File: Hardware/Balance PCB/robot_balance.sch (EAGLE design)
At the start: 54 parts, among them P1 10118194-0001LF, Q1 16Mhz

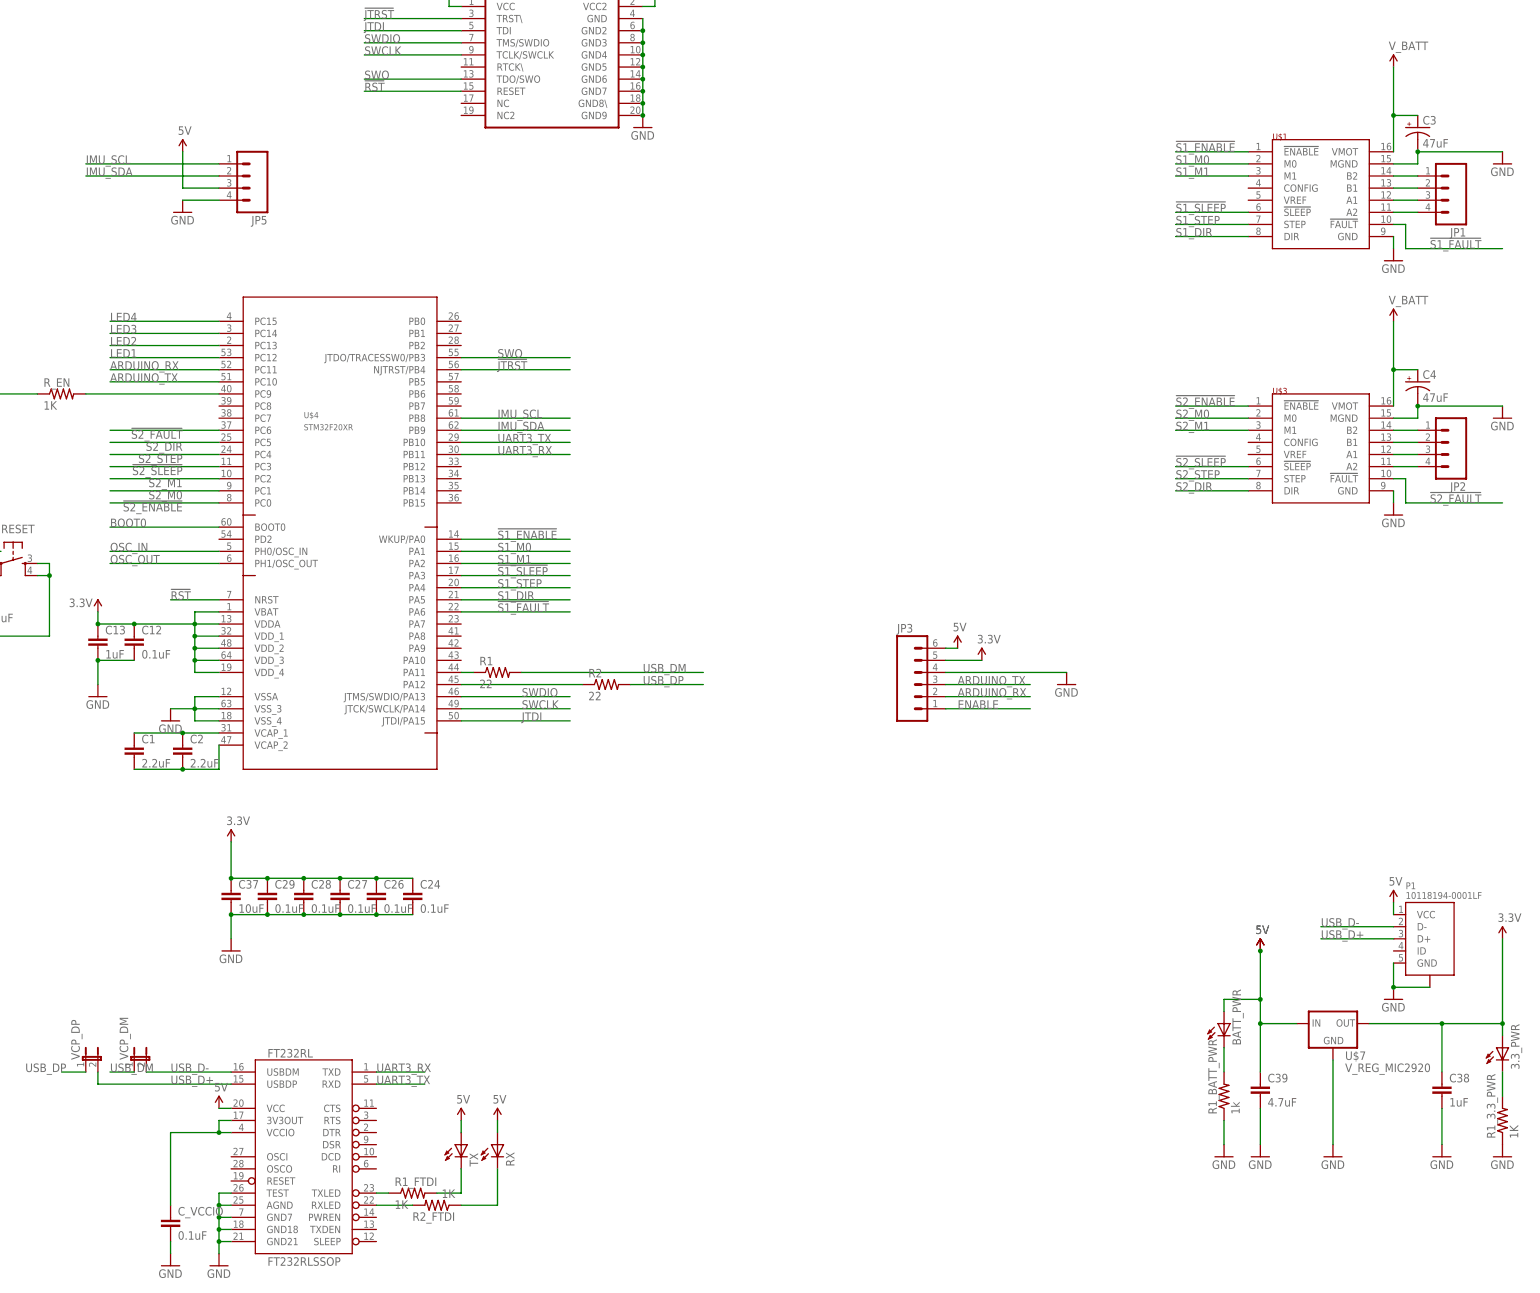
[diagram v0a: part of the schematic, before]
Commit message: Moved MPU to middle of board
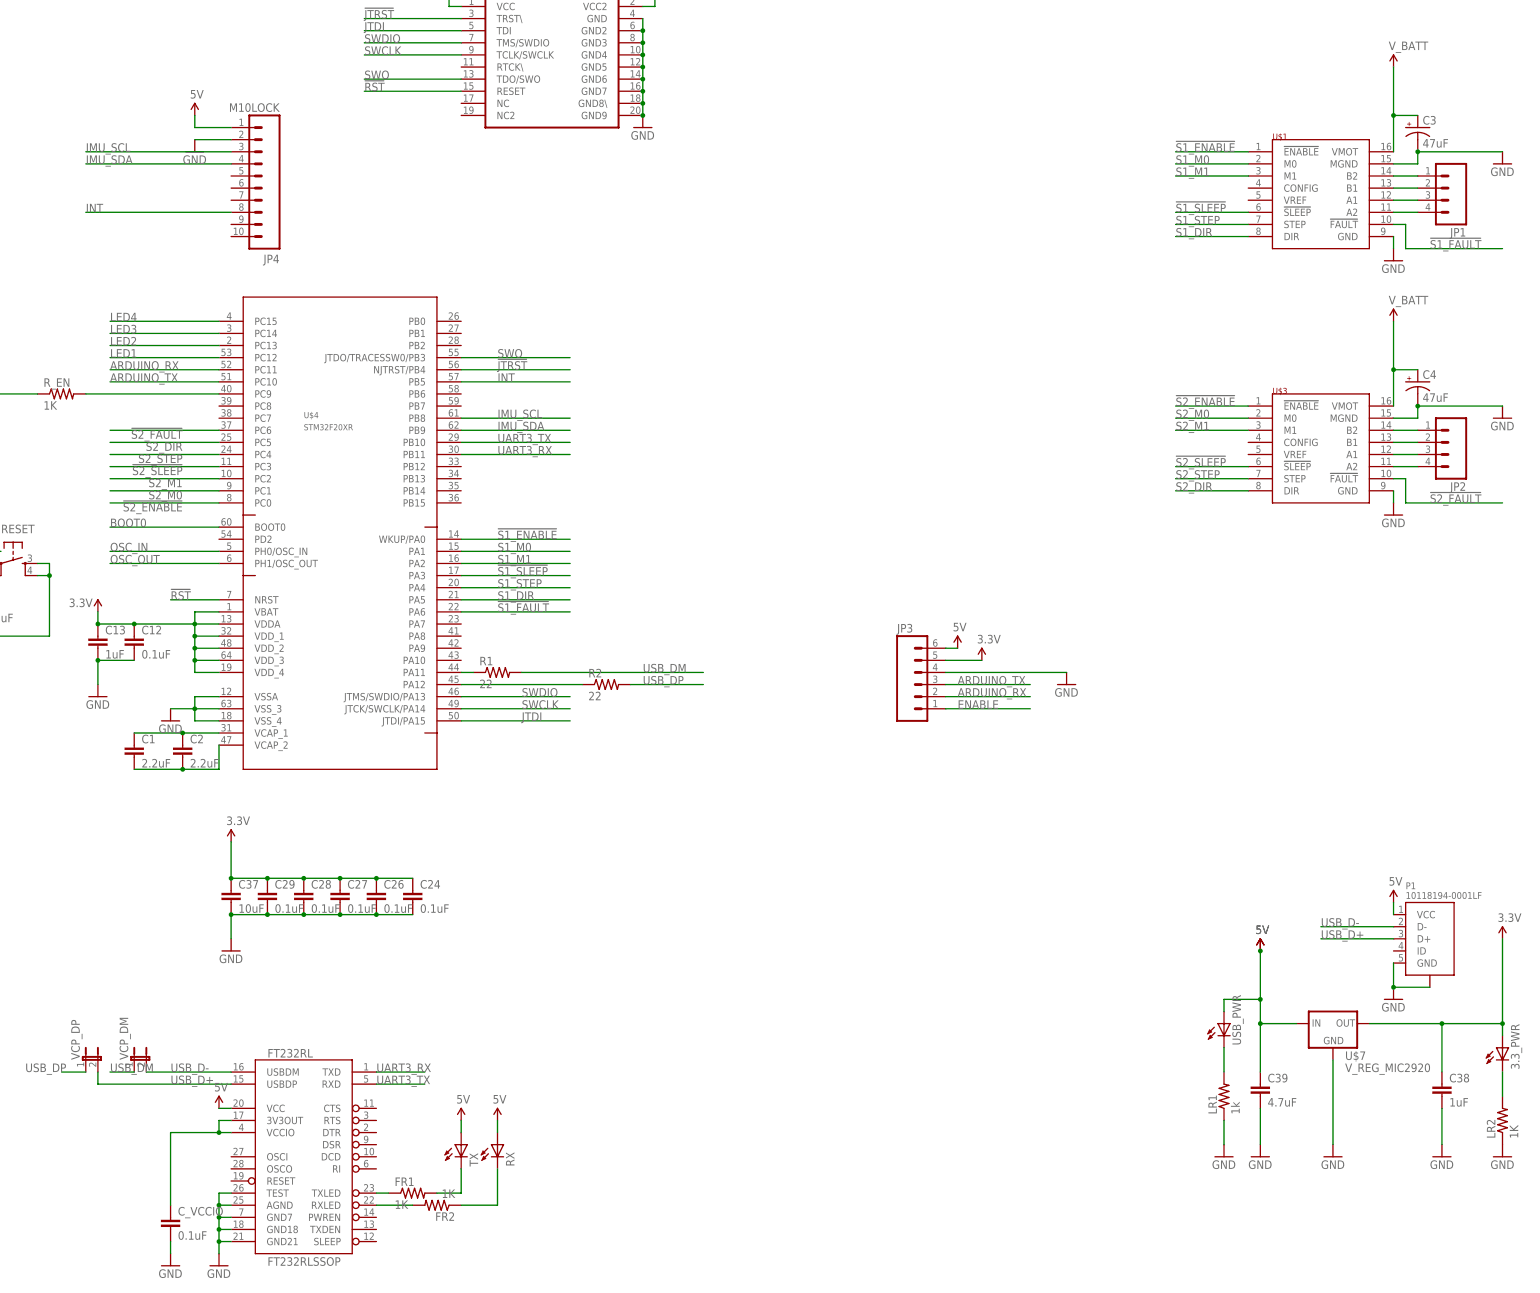
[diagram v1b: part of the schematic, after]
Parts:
- removed BATT_PWR: (no value), LilyPad-Wearables:LED1206
- removed JP5: (no value), SparkFun-Connectors:M04POLAR_LOCK
- added JP4: M10LOCK, SparkFun-Connectors:M10LOCK
- added USB_PWR: (no value), adafruit:LEDCHIP-LED0805
- renumbered R1_3.3_PWR to LR2, R1_BATT_PWR to LR1, R1_FTDI to FR1, R2_FTDI to FR2
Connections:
- new net INT: JP4.8, U$4.PB5
- net 5V: now also JP4.1, USB_PWR.A; no longer BATT_PWR.A, JP5.3
- net GND: now also JP4.2; no longer JP5.4
- net IMU_SCL: now also JP4.3; no longer JP5.1
- net IMU_SDA: now also JP4.4; no longer JP5.2
- net N$19: now also USB_PWR.C; no longer BATT_PWR.C
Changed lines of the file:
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@@
 <part name="GND20" library="SparkFun-Aesthetics" deviceset="GND" device=""/>
 <part name="SUPPLY18" library="SparkFun-Aesthetics" deviceset="3.3V" device=""/>
-<part name="BATT_PWR" library="LilyPad-Wearables" deviceset="LED" device="1206"/>
+<part name="USB_PWR" library="adafruit" deviceset="LED" device="CHIP-LED0805"/>
 <part name="3.3_PWR" library="LilyPad-Wearables" deviceset="LED" device="1206"/>
 <part name="GND22" library="SparkFun-Aesthetics" deviceset="GND" device=""/>
 <part name="GND23" library="SparkFun-Aesthetics" deviceset="GND" device=""/>
-<part name="R1_3.3_PWR" library="SparkFun-Resistors" deviceset="RESISTOR" device="0805-RES" value="1K"/>
-<part name="R1_BATT_PWR" library="SparkFun-Resistors" deviceset="RESISTOR" device="0805-RES" value="1k"/>
+<part name="LR2" library="SparkFun-Resistors" deviceset="RESISTOR" device="0805-RES" value="1K"/>
+<part name="LR1" library="SparkFun-Resistors" deviceset="RESISTOR" device="0805-RES" value="1k"/>
 <part name="U$7" library="SparkFun-PowerIC" deviceset="V_REG_MIC2920" device=""/>
 <part name="C39" library="SparkFun-Capacitors" deviceset="22UF-6.3V-20%(0805)" device="" value="4.7uF"/>
@@
 <part name="GND6" library="SparkFun-Aesthetics" deviceset="GND" device=""/>
 <part name="GND7" library="SparkFun-Aesthetics" deviceset="GND" device=""/>
-<part name="JP5" library="SparkFun-Connectors" deviceset="M04" device="POLAR_LOCK"/>
 <part name="GND9" library="SparkFun-Aesthetics" deviceset="GND" device=""/>
 <part name="U$4" library="stm32F" deviceset="STM32F20XR" device=""/>
@@
 <part name="SUPPLY10" library="SparkFun-Aesthetics" deviceset="5V" device=""/>
 <part name="SUPPLY11" library="SparkFun-Aesthetics" deviceset="5V" device=""/>
-<part name="R1_FTDI" library="SparkFun-Passives" deviceset="RESISTOR" device="0603-RES" value="1K"/>
-<part name="R2_FTDI" library="SparkFun-Passives" deviceset="RESISTOR" device="0603-RES" value="1K"/>
+<part name="FR1" library="SparkFun-Passives" deviceset="RESISTOR" device="0603-RES" value="1K"/>
+<part name="FR2" library="SparkFun-Passives" deviceset="RESISTOR" device="0603-RES" value="1K"/>
 <part name="GND11" library="SparkFun-Aesthetics" deviceset="GND" device=""/>
 <part name="C_VCCIO" library="SparkFun-Capacitors" deviceset="CAP" device="0603-CAP" value="0.1uF"/>
@@
 <part name="R1" library="SparkFun-Passives" deviceset="RESISTOR" device="0805-RES" value="22"/>
 <part name="R2" library="SparkFun-Passives" deviceset="RESISTOR" device="0805-RES" value="22"/>
+<part name="JP4" library="SparkFun-Connectors" deviceset="M10" device="LOCK"/>
 </parts>
 <sheets>
@@
 <instance part="GND20" gate="1" x="299.72" y="-172.72"/>
 <instance part="SUPPLY18" gate="G$1" x="335.28" y="-127"/>
-<instance part="BATT_PWR" gate="G$1" x="276.86" y="-144.78"/>
+<instance part="USB_PWR" gate="G$1" x="276.86" y="-144.78"/>
 <instance part="3.3_PWR" gate="G$1" x="335.28" y="-149.86"/>
 <instance part="GND22" gate="1" x="276.86" y="-172.72"/>
 <instance part="GND23" gate="1" x="335.28" y="-172.72"/>
-<instance part="R1_3.3_PWR" gate="G$1" x="335.28" y="-165.1" rot="R90"/>
-<instance part="R1_BATT_PWR" gate="G$1" x="276.86" y="-160.02" rot="R90"/>
+<instance part="LR2" gate="G$1" x="335.28" y="-165.1" rot="R90"/>
+<instance part="LR1" gate="G$1" x="276.86" y="-160.02" rot="R90"/>
 <instance part="U$7" gate="G$1" x="299.72" y="-144.78"/>
 <instance part="C39" gate="G$1" x="284.48" y="-160.02"/>
@@
 <instance part="GND6" gate="1" x="312.42" y="-139.7"/>
 <instance part="GND7" gate="1" x="243.84" y="-73.66"/>
-<instance part="JP5" gate="G$1" x="71.12" y="33.02" rot="R180"/>
-<instance part="GND9" gate="1" x="58.42" y="25.4"/>
+<instance part="GND9" gate="1" x="60.96" y="38.1"/>
 <instance part="U$4" gate="G$1" x="106.68" y="-45.72"/>
 <instance part="GND1" gate="1" x="55.88" y="-81.28"/>
@@
 <instance part="SUPPLY10" gate="G$1" x="116.84" y="-165.1"/>
 <instance part="SUPPLY11" gate="G$1" x="124.46" y="-165.1"/>
-<instance part="R1_FTDI" gate="G$1" x="106.68" y="-180.34"/>
-<instance part="R2_FTDI" gate="G$1" x="111.76" y="-182.88" rot="R180"/>
+<instance part="FR1" gate="G$1" x="106.68" y="-180.34"/>
+<instance part="FR2" gate="G$1" x="111.76" y="-182.88" rot="R180"/>
 <instance part="GND11" gate="1" x="55.88" y="-195.58"/>
 <instance part="C_VCCIO" gate="G$1" x="55.88" y="-187.96"/>
@@
 <instance part="SUPPLY7" gate="G$1" x="284.48" y="-129.54"/>
 <instance part="SUPPLY8" gate="G$1" x="220.98" y="-66.04"/>
-<instance part="SUPPLY6" gate="G$1" x="58.42" y="38.1"/>
+<instance part="SUPPLY6" gate="G$1" x="60.96" y="45.72"/>
 <instance part="GND10" gate="1" x="66.04" y="-195.58"/>
 <instance part="U$2" gate="G$1" x="121.92" y="43.18"/>
@@
 <instance part="R1" gate="G$1" x="124.46" y="-71.12"/>
 <instance part="R2" gate="G$1" x="147.32" y="-73.66"/>
+<instance part="JP4" gate="G$1" x="78.74" y="25.4" rot="R180"/>
 </instances>
 <busses>
@@
 </segment>
 <segment>
-<pinref part="R1_3.3_PWR" gate="G$1" pin="1"/>
+<pinref part="LR2" gate="G$1" pin="1"/>
 <pinref part="GND23" gate="1" pin="GND"/>
 </segment>
 <segment>
-<pinref part="R1_BATT_PWR" gate="G$1" pin="1"/>
+<pinref part="LR1" gate="G$1" pin="1"/>
 <pinref part="GND22" gate="1" pin="GND"/>
 <wire x1="276.86" y1="-165.1" x2="276.86" y2="-170.18" width="0.1524" layer="91"/>
@@
 <segment>
 <pinref part="GND9" gate="1" pin="GND"/>
-<pinref part="JP5" gate="G$1" pin="4"/>
-<wire x1="58.42" y1="27.94" x2="66.04" y2="27.94" width="0.1524" layer="91"/>
+<wire x1="60.96" y1="40.64" x2="68.58" y2="40.64" width="0.1524" layer="91"/>
+<pinref part="JP4" gate="G$1" pin="2"/>
 </segment>
 <segment>
@@
 <segment>
 <pinref part="3.3_PWR" gate="G$1" pin="C"/>
-<pinref part="R1_3.3_PWR" gate="G$1" pin="2"/>
+<pinref part="LR2" gate="G$1" pin="2"/>
 <wire x1="335.28" y1="-160.02" x2="335.28" y2="-154.94" width="0.1524" layer="91"/>
 </segment>
@@
 <net name="N$19" class="1">
 <segment>
-<pinref part="BATT_PWR" gate="G$1" pin="C"/>
-<pinref part="R1_BATT_PWR" gate="G$1" pin="2"/>
+<pinref part="USB_PWR" gate="G$1" pin="C"/>
+<pinref part="LR1" gate="G$1" pin="2"/>
 <wire x1="276.86" y1="-154.94" x2="276.86" y2="-149.86" width="0.1524" layer="91"/>
 </segment>
@@
 <net name="IMU_SCL" class="0">
 <segment>
-<pinref part="JP5" gate="G$1" pin="1"/>
-<wire x1="66.04" y1="35.56" x2="38.1" y2="35.56" width="0.1524" layer="91"/>
-<label x="38.1" y="35.56" size="1.778" layer="95"/>
+<wire x1="68.58" y1="38.1" x2="38.1" y2="38.1" width="0.1524" layer="91"/>
+<label x="38.1" y="38.1" size="1.778" layer="95"/>
+<pinref part="JP4" gate="G$1" pin="3"/>
 </segment>
 <segment>
@@
 <net name="IMU_SDA" class="0">
 <segment>
-<pinref part="JP5" gate="G$1" pin="2"/>
-<wire x1="66.04" y1="33.02" x2="38.1" y2="33.02" width="0.1524" layer="91"/>
-<label x="38.1" y="33.02" size="1.778" layer="95"/>
+<wire x1="68.58" y1="35.56" x2="38.1" y2="35.56" width="0.1524" layer="91"/>
+<label x="38.1" y="35.56" size="1.778" layer="95"/>
+<pinref part="JP4" gate="G$1" pin="4"/>
 </segment>
 <segment>
@@
 <wire x1="292.1" y1="-144.78" x2="284.48" y2="-144.78" width="0.1524" layer="91"/>
 <wire x1="284.48" y1="-144.78" x2="284.48" y2="-139.7" width="0.1524" layer="91"/>
-<pinref part="BATT_PWR" gate="G$1" pin="A"/>
+<pinref part="USB_PWR" gate="G$1" pin="A"/>
 <wire x1="276.86" y1="-142.24" x2="276.86" y2="-139.7" width="0.1524" layer="91"/>
 <wire x1="276.86" y1="-139.7" x2="284.48" y2="-139.7" width="0.1524" layer="91"/>
@@
 </segment>
 <segment>
-<pinref part="JP5" gate="G$1" pin="3"/>
-<wire x1="66.04" y1="30.48" x2="58.42" y2="30.48" width="0.1524" layer="91"/>
-<wire x1="58.42" y1="30.48" x2="58.42" y2="38.1" width="0.1524" layer="91"/>
+<wire x1="68.58" y1="43.18" x2="60.96" y2="43.18" width="0.1524" layer="91"/>
+<wire x1="60.96" y1="43.18" x2="60.96" y2="45.72" width="0.1524" layer="91"/>
 <pinref part="SUPPLY6" gate="G$1" pin="5V"/>
+<pinref part="JP4" gate="G$1" pin="1"/>
 </segment>
 <segment>
@@
 <pinref part="TX" gate="G$1" pin="C"/>
 <wire x1="116.84" y1="-175.26" x2="116.84" y2="-180.34" width="0.1524" layer="91"/>
-<pinref part="R1_FTDI" gate="G$1" pin="2"/>
+<pinref part="FR1" gate="G$1" pin="2"/>
 <wire x1="111.76" y1="-180.34" x2="116.84" y2="-180.34" width="0.1524" layer="91"/>
 </segment>
@@
 <segment>
 <pinref part="FT232RL" gate="G$1" pin="TXLED"/>
-<pinref part="R1_FTDI" gate="G$1" pin="1"/>
+<pinref part="FR1" gate="G$1" pin="1"/>
 <wire x1="99.06" y1="-180.34" x2="101.6" y2="-180.34" width="0.1524" layer="91"/>
 </segment>
@@
 <segment>
 <pinref part="FT232RL" gate="G$1" pin="RXLED"/>
-<pinref part="R2_FTDI" gate="G$1" pin="2"/>
+<pinref part="FR2" gate="G$1" pin="2"/>
 <wire x1="99.06" y1="-182.88" x2="106.68" y2="-182.88" width="0.1524" layer="91"/>
 </segment>
@@
 <net name="N$11" class="1">
 <segment>
-<pinref part="R2_FTDI" gate="G$1" pin="1"/>
+<pinref part="FR2" gate="G$1" pin="1"/>
 <wire x1="116.84" y1="-182.88" x2="124.46" y2="-182.88" width="0.1524" layer="91"/>
 <pinref part="RX" gate="G$1" pin="C"/>
@@
 </segment>
 </net>
+<net name="INT" class="0">
+<segment>
+<pinref part="JP4" gate="G$1" pin="8"/>
+<wire x1="68.58" y1="25.4" x2="38.1" y2="25.4" width="0.1524" layer="91"/>
+<label x="38.1" y="25.4" size="1.778" layer="95"/>
+</segment>
+<segment>
+<pinref part="U$4" gate="G$1" pin="PB5"/>
+<wire x1="116.84" y1="-10.16" x2="139.7" y2="-10.16" width="0.1524" layer="91"/>
+<label x="124.46" y="-10.16" size="1.778" layer="95"/>
+</segment>
+</net>
